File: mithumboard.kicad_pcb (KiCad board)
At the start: 2 copper layers, 28 parts, among them J1 MJ-4PP-9, J2 MJ-4PP-9, J3 MJ-4PP-9, J4 MJ-4PP-9, SW1 SW_Push, SW10 SW_Push, SW11 SW_Push, SW12 SW_Push, SW13 SW_Push, SW14 SW_Push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

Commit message: 不要になったピラーを除去
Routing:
- net R2C3: vias 2 -> 0
- net GND: vias 14 -> 15

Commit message: 穴開けてみた
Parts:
- added H1: MountingHole, MountingHole:MountingHole_3.2mm_M3, B.Cu at (71.5, 69.0)
- added H2: MountingHole, MountingHole:MountingHole_3.2mm_M3, B.Cu at (127.2, 108.0)
- added H3: MountingHole, MountingHole:MountingHole_3.2mm_M3, B.Cu at (107.6, 69.0)
- added H4: MountingHole, MountingHole:MountingHole_3.2mm_M3, B.Cu at (71.5, 108.0)
- added H5: MountingHole, MountingHole:MountingHole_3.2mm_M3, B.Cu at (160.8, 69.0)
- added H6: MountingHole, MountingHole:MountingHole_3.2mm_M3, B.Cu at (160.8, 108.0)
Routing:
- net SDA: track 98.3 -> 96.5 mm
- net R3C4: track 23.7 -> 24.5 mm
- net R1C3: track 63.0 -> 63.5 mm

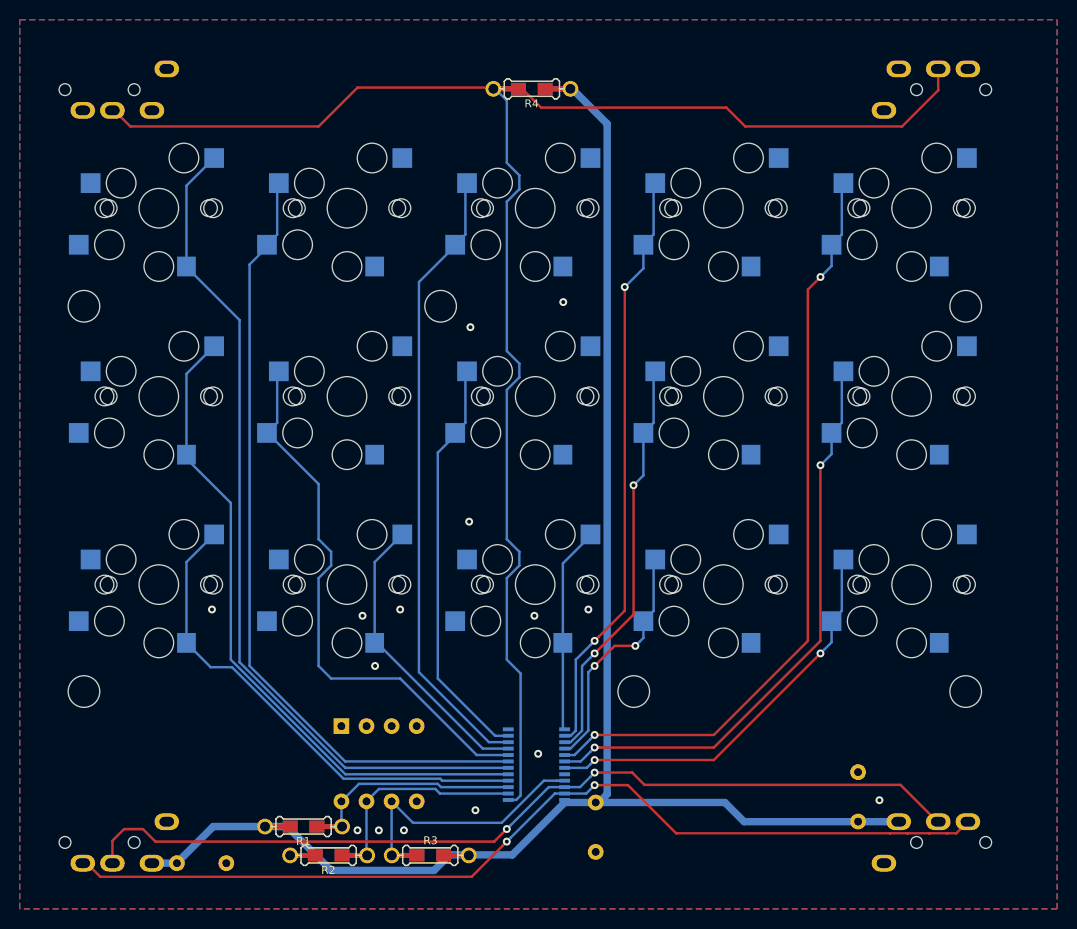
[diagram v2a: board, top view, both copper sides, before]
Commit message: MCP23017 に変更。配線開始。
キースイッチ以外は一応引けた。はず。
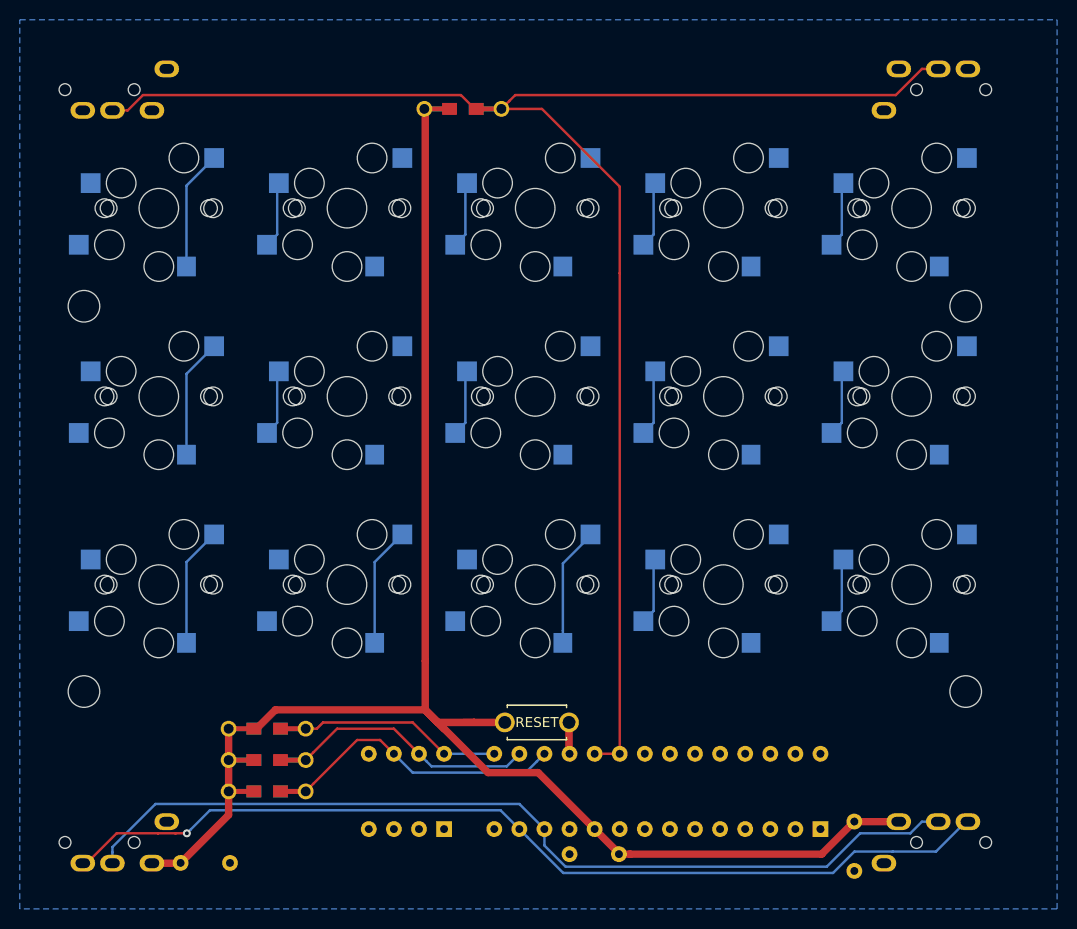
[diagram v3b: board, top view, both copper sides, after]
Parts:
- removed H2, H3: MountingHole, MountingHole:MountingHole_3.2mm_M3
- added SW17: SW_PUSH, kbd:ResetSW_1side, F.Cu at (117.3, 111.1)
- C1, C2, C3: footprint Capacitor_THT:C_Disc_D6.0mm_W4.4mm_P5.00mm -> Capacitor_THT:C_Disc_D6.0mm_W2.5mm_P5.00mm
- R1, R2, R3, R4: moved to B.Cu
- U1: value TCA9555PWR -> MCP23017_SP; footprint Package_SO:TSSOP-24_4.4x7.8mm_P0.65mm -> Package_DIP:DIP-28_W7.62mm
- moved U1 29.5 mm to (146.1, 121.9), turned to 90 degrees
- moved R3 17.7 mm to (90.0, 118.1), turned to 0 degrees
- moved SW16 14.7 mm to (108.0, 121.9), turned to 90 degrees
- moved R2 11.5 mm to (90.0, 114.9)
- moved R1 10.6 mm to (90.0, 111.8)
- moved R4 7.27 mm to (109.9, 49.0), turned to 180 degrees
- moved C1 2.66 mm to (120.7, 124.5), turned to 0 degrees
- moved C2 0.38 mm to (149.5, 121.2), turned to 270 degrees
- moved C3 0.38 mm to (81.3, 125.3)
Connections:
- R1 pad 1: A2 -> A0
- R3 pad 1: A0 -> A2
- SW16 pad 6: A0 -> A2
- SW16 pad 8: A2 -> A0
- U1 pad 1: INT -> R3C1
- U1 pad 10: R1C3 -> 3.3V
- U1 pad 11: R2C3 -> Net-(U1-Pad11)
- U1 pad 12: GND -> SCL
- U1 pad 13: R3C3 -> SDA
- U1 pad 14: R1C4 -> Net-(U1-Pad14)
- U1 pad 15: R2C4 -> A0
- U1 pad 16: R3C4 -> A1
- U1 pad 17: R1C5 -> A2
- U1 pad 18: R2C5 -> RESET
- U1 pad 19: R3C5 -> INT
- U1 pad 2: A1 -> R2C1
- U1 pad 20: Net-(U1-Pad20) -> INT
- U1 pad 21: A0 -> R3C3
- U1 pad 22: SCL -> R1C4
- U1 pad 23: SDA -> R2C4
- U1 pad 24: 3.3V -> R3C4
- U1 pad 3: A2 -> R1C1
- U1 pad 4: R3C1 -> R1C2
- U1 pad 5: R2C1 -> R2C2
- U1 pad 6: R1C1 -> R3C2
- U1 pad 7: R1C2 -> R1C3
- U1 pad 8: R2C2 -> R2C3
- U1 pad 9: R3C2 -> GND
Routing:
- net R1C1: track 86.0 -> 12.1 mm
- net R1C2: track 80.3 -> 6.74 mm
- net R1C5: track 77.2 -> 6.74 mm, vias 2 -> 0
- net R1C3: track 63.5 -> 6.74 mm
- net R2C1: track 67.6 -> 12.1 mm
- net R1C4: track 60.1 -> 6.74 mm, vias 2 -> 0
- net R2C5: track 59.2 -> 6.74 mm, vias 2 -> 0
- net R2C2: track 56.5 -> 6.74 mm
- net R3C1: track 50.6 -> 12.2 mm
- net R2C3: track 42.1 -> 6.93 mm
- net R2C4: track 41.7 -> 6.74 mm, vias 2 -> 0
- net R3C5: track 41.2 -> 6.74 mm, vias 2 -> 0
- net R3C4: track 24.5 -> 6.74 mm, vias 2 -> 0
- net R3C2: track 30.1 -> 12.4 mm
- net R3C3: track 21.3 -> 12.1 mm
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- removed copper zone on F.Cu, net GND

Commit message: キースイッチまで配線終わり
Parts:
- removed H5, H6: MountingHole, MountingHole:MountingHole_3.2mm_M3
- added H2: MountingHole, MountingHole:MountingHole_3.2mm_M3, F.Cu at (72.1, 107.6)
- added H3: MountingHole, MountingHole:MountingHole_3.2mm_M3, F.Cu at (159.8, 69.0)
- moved H4 88.3 mm to (159.8, 107.6)
- moved H1 0.64 mm to (72.1, 69.0)
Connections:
- SW10 pad 1: R1C4 -> GND
- SW10 pad 2: GND -> R1C4
- SW11 pad 1: R2C4 -> GND
- SW11 pad 2: GND -> R2C4
- SW12 pad 1: R3C4 -> GND
- SW12 pad 2: GND -> R3C4
- SW13 pad 1: R1C5 -> GND
- SW13 pad 2: GND -> R1C5
- SW4 pad 1: R1C2 -> GND
- SW4 pad 2: GND -> R1C2
- SW5 pad 1: R2C2 -> GND
- SW5 pad 2: GND -> R2C2
- SW7 pad 1: R1C3 -> GND
- SW7 pad 2: GND -> R1C3
- SW8 pad 1: R2C3 -> GND
- SW8 pad 2: GND -> R2C3
- U1 pad 1: R3C1 -> R1C3
- U1 pad 2: R2C1 -> R2C3
- U1 pad 22: R1C4 -> Net-(U1-Pad22)
- U1 pad 23: R2C4 -> R3C4
- U1 pad 24: R3C4 -> R2C4
- U1 pad 25: R1C5 -> R1C4
- U1 pad 28: Net-(U1-Pad28) -> R1C5
- U1 pad 3: R1C1 -> R1C2
- U1 pad 4: R1C2 -> R2C2
- U1 pad 5: R2C2 -> R3C2
- U1 pad 6: R3C2 -> R1C1
- U1 pad 7: R1C3 -> R2C1
- U1 pad 8: R2C3 -> R3C1
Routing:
- net R1C1: track 12.1 -> 106.5 mm
- net R1C2: track 6.74 -> 96.1 mm
- net R1C3: track 6.74 -> 84.3 mm
- net R2C1: track 12.1 -> 85.6 mm
- net R1C5: track 6.74 -> 79.9 mm
- net R2C2: track 6.74 -> 76.0 mm
- net R1C4: track 6.74 -> 66.5 mm
- net R2C3: track 6.93 -> 64.2 mm
- net R3C1: track 12.2 -> 68.0 mm
- net R3C2: track 12.4 -> 55.7 mm
- net R2C4: track 6.74 -> 48.0 mm
- net R2C5: track 6.74 -> 41.8 mm
- net R3C4: track 6.74 -> 25.7 mm
- net R3C5: track 6.74 -> 21.7 mm
- net R3C3: track 12.1 -> 26.8 mm
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- added copper zone on F.Cu, net GND

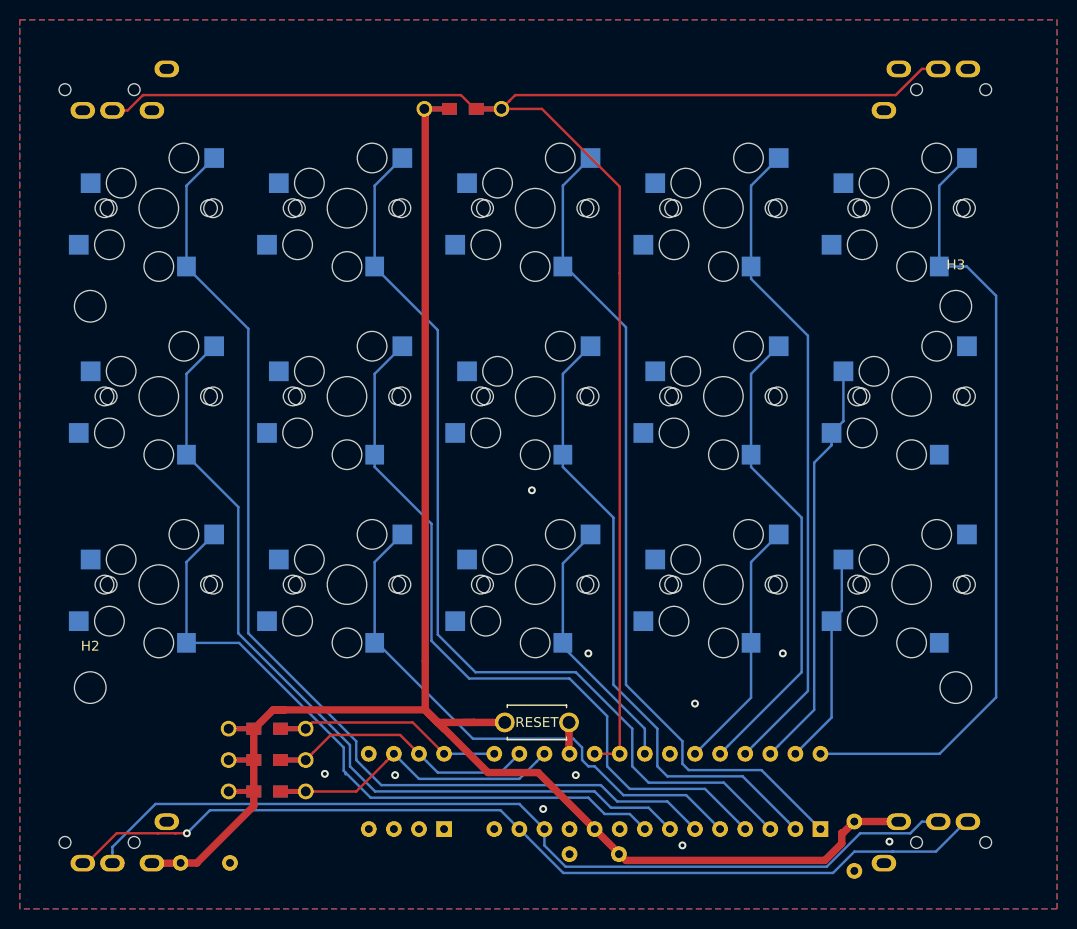
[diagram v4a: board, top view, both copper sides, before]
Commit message: MCP23017 に置き換えて線を引きなおし
これであってるのかさっぱりわからん。
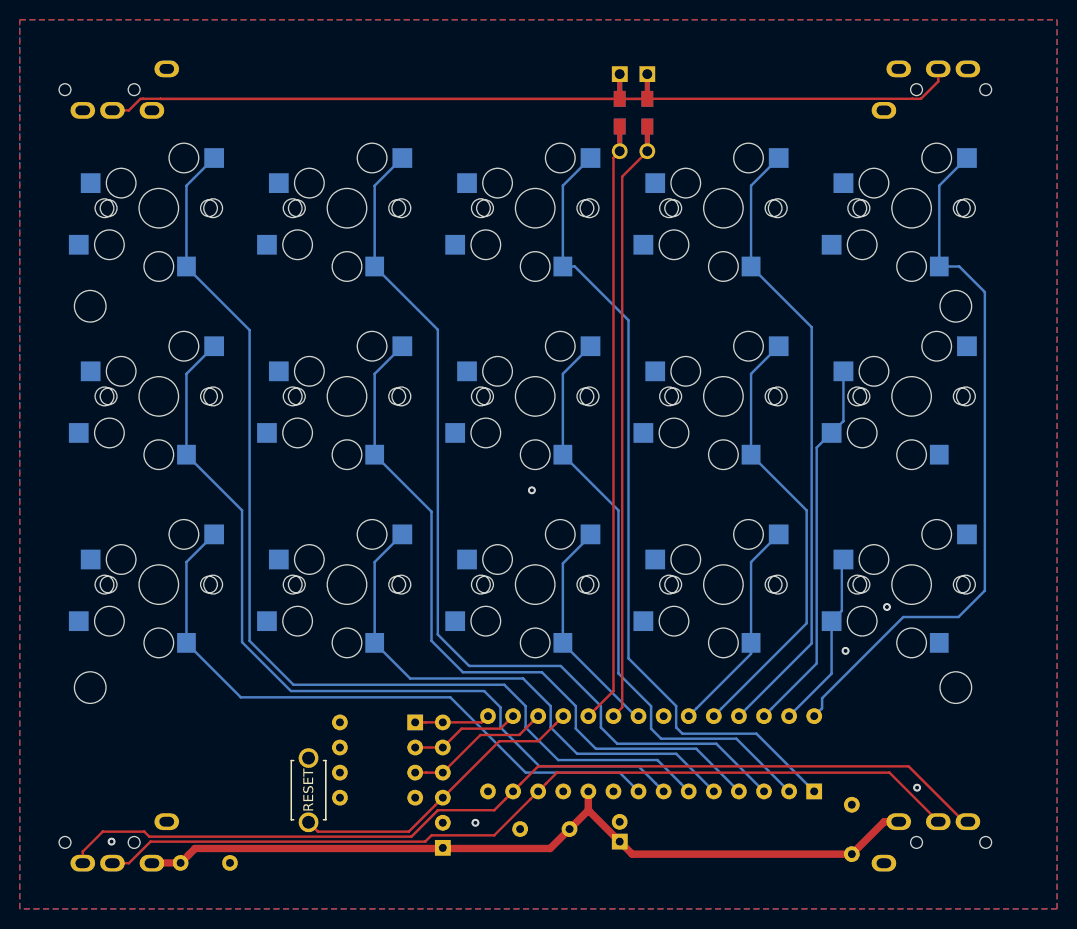
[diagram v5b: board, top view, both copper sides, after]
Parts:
- removed R1, R2, R3: 1M, Keebio-Parts:Resistor-Hybrid
- removed R4: 10k, Keebio-Parts:Resistor-Hybrid
- added C4: 1u, Capacitor_THT:C_Disc_D6.0mm_W2.5mm_P5.00mm, B.Cu at (149.2, 124.5)
- added D1: D, Keebio-Parts:Diode-dual, B.Cu at (128.5, 49.4)
- added D2: D, Keebio-Parts:Diode-dual, B.Cu at (125.7, 49.4)
- added RN1: 10k, Resistor_THT:R_Array_SIP6, B.Cu at (107.8, 123.8)
- C1: value 100n -> 0.1u
- C2: value 1u -> 47u/16V; footprint Capacitor_THT:C_Disc_D6.0mm_W2.5mm_P5.00mm -> Capacitor_THT:CP_Radial_D5.0mm_P2.00mm
- H2, H3: moved to B.Cu
- SW16: footprint Button_Switch_THT:SW_DIP_SPSTx04_Slide_9.78x12.34mm_W7.62mm_P2.54mm -> Button_Switch_THT:SW_DIP_SPSTx04_Slide_6.7x11.72mm_W7.62mm_P2.54mm_LowProfile
- SW17: value SW_PUSH -> SW_Push; footprint kbd:ResetSW_1side -> kbd:ResetSW
- moved SW17 24.1 mm to (94.2, 118.0), turned to 270 degrees
- moved C2 23.8 mm to (125.7, 123.2), turned to 90 degrees
- moved SW16 11.2 mm to (105.0, 111.1), turned to 180 degrees
- moved U1 3.86 mm to (145.4, 118.1)
- moved C1 2.54 mm to (120.7, 121.9), turned to 180 degrees
- turned H3 to 270 degrees
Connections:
- C1 pad 1: GND -> VCC
- C1 pad 2: 3.3V -> GND
- C2 pad 1: 3.3V -> VCC
- C3 pad 1: 3.3V -> VCC
- J1 pad D: 3.3V -> VCC
- J2 pad D: 3.3V -> VCC
- SW16 pad 1: GND -> A0
- SW16 pad 2: GND -> A1
- SW16 pad 3: GND -> A2
- SW16 pad 5: Net-(SW16-Pad5) -> GND
- SW16 pad 6: A2 -> GND
- SW16 pad 7: A1 -> GND
- SW16 pad 8: A0 -> GND
- SW17 pad 2: 3.3V -> GND
- U1 pad 10: 3.3V -> VCC
- U1 pad 19: INT -> INTB
- U1 pad 20: INT -> INTA
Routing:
- net 3.3V: track 170.3 -> 0.00 mm
- net VCC: track 0.00 -> 83.8 mm
- net INT: track 159.1 -> 86.1 mm
- net INTA: track 0.00 -> 58.6 mm
- net INTB: track 0.00 -> 58.5 mm
- net RESET: track 3.20 -> 31.0 mm
- net A1: track 25.0 -> 11.2 mm
- net A2: track 27.8 -> 14.8 mm
- net A0: track 20.7 -> 7.63 mm
- net R1C5: track 79.9 -> 71.2 mm
- net R2C3: track 64.2 -> 60.2 mm
- net R2C2: track 76.0 -> 72.1 mm
- net R3C1: track 68.0 -> 64.2 mm
- net R3C4: track 25.7 -> 22.2 mm
- net R3C5: track 21.7 -> 18.1 mm
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
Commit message: INT 周りを修正
基本、INTA だけを使用。
いざというときに INTB も使えるようにしておく。
また、プルアップの抵抗も使わない予定だけれど、念のためパターンは置いておくことにする。
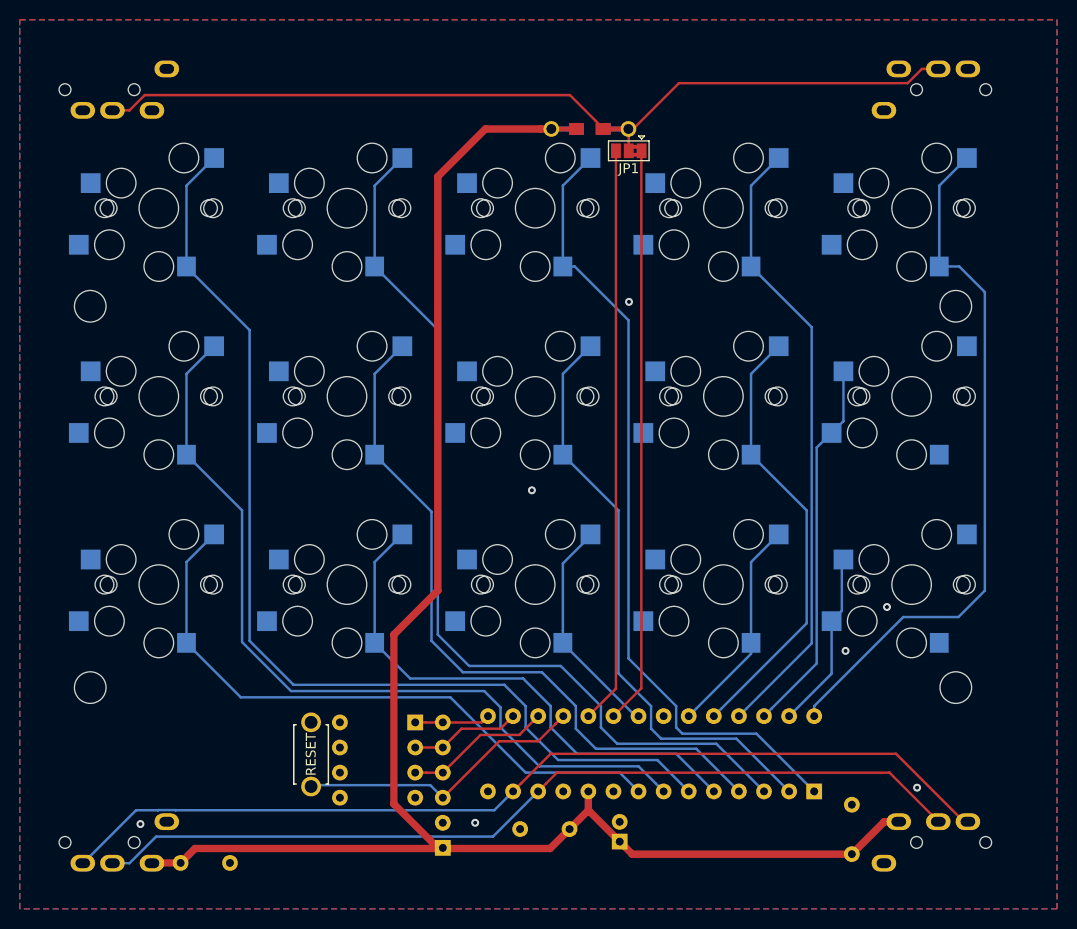
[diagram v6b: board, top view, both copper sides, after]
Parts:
- removed D1, D2: D, Keebio-Parts:Diode-dual
- added JP1: SolderJumper_3_Bridged12, Jumper:SolderJumper-3_P1.3mm_Bridged2Bar12_Pad1.0x1.5mm, F.Cu at (126.6, 53.3)
- added R1: R, Keebio-Parts:Resistor-Hybrid, B.Cu at (122.7, 51.1)
- moved SW17 3.63 mm to (94.5, 114.4)
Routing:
- net VCC: track 83.8 -> 169.5 mm
- net INT: track 86.1 -> 89.2 mm
- net RESET: track 31.0 -> 29.5 mm
- net GND: vias 6 -> 7
